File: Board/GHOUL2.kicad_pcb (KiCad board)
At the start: 2 copper layers, 105.1 x 68.6 mm, 16 parts, among them J1 Conn_01x02, Q1 IRF540N, Q2 IRF540N, U1 Teensy3.5_All_Pins, U10 GHOULIMU, U2 LM7805_TO220, U3 BMP280, U4 Feedback_Serv, U5 LM1084-ADJ, U6 NichromeConnector, U7 Ultimate_GPS_Breakout_v3, U8 Xbee, U9 NichromeConnector

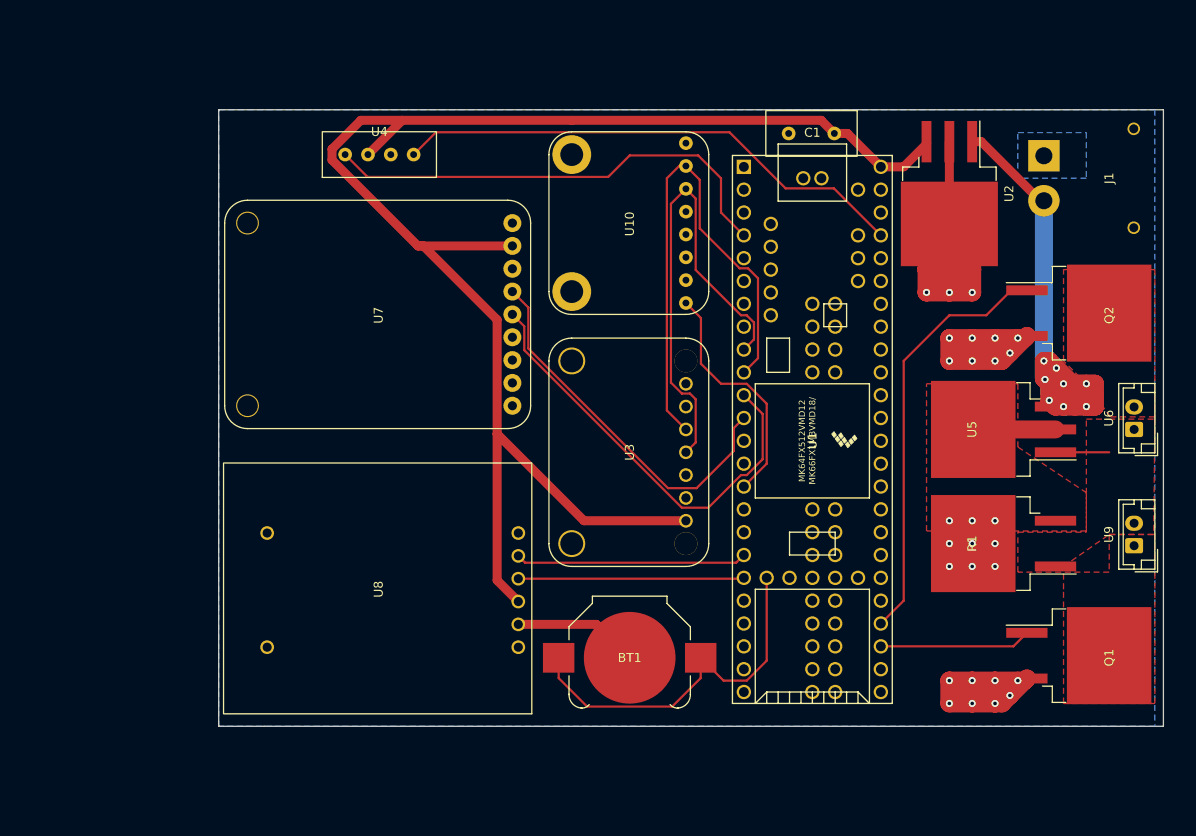
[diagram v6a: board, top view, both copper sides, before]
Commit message: Rounded Corners but not mounting holes
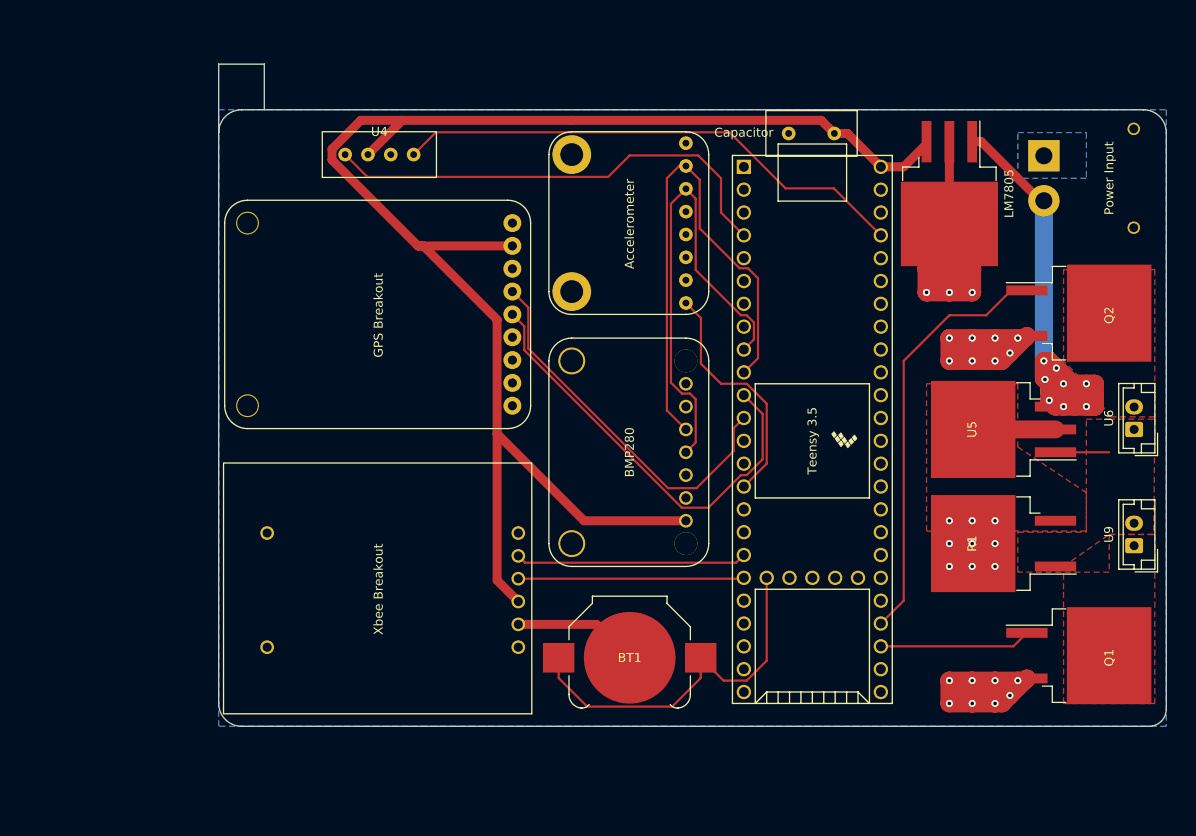
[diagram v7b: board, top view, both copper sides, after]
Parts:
- GPS Breakout: renamed from U7
- Power Input: renamed from J1
- Teensy 3.5: renamed from U1
- Xbee Breakout: renamed from U8
- renumbered U10 to Accelerometer, U3 to BMP280, C1 to Capacitor, U2 to LM7805
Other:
- board size 105.1 x 68.6 mm -> 105.4 x 73.7 mm

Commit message: Added mounting, labels, rounded corners
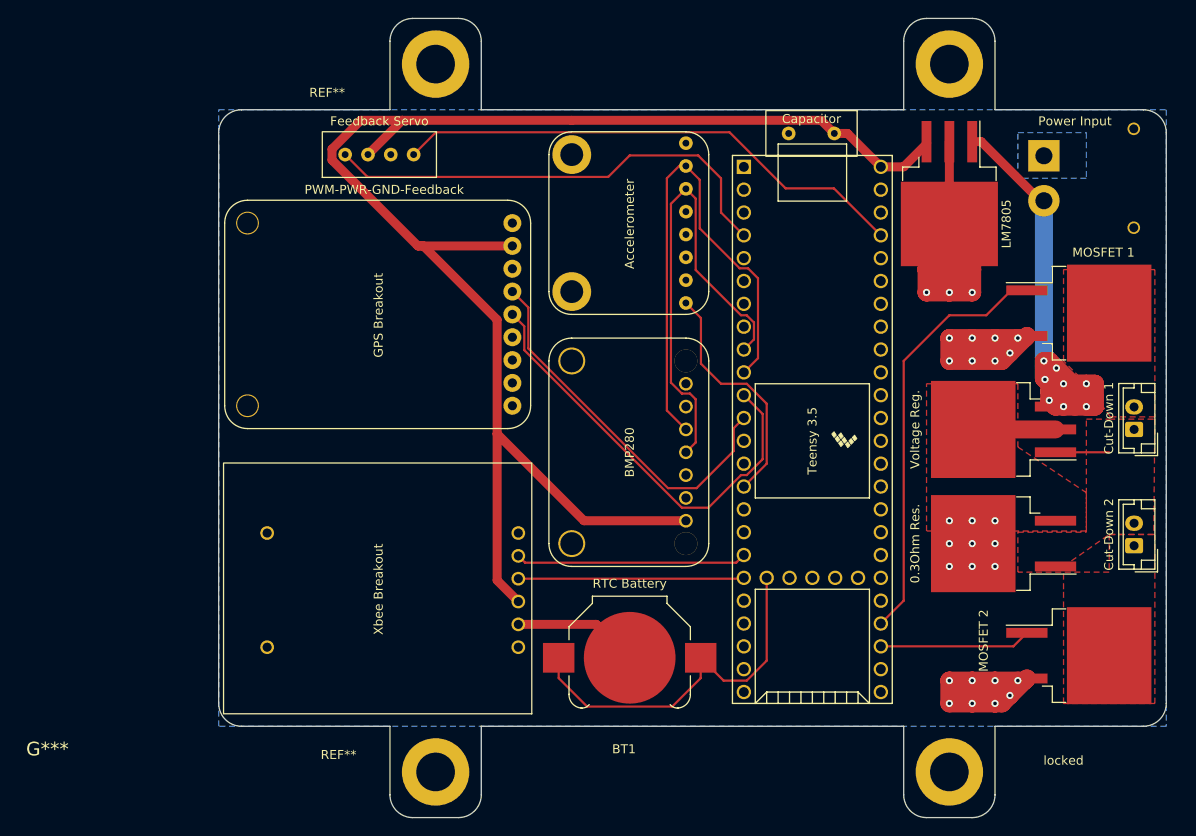
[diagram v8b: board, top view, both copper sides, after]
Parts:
- added ?: , , F.Cu at (175.3, 63.5)
- added G***: LOGO, GHOULFootPrints:GHOULFootprint, F.Cu at (123.2, 109.2)
- added REF**: MountingHole_4.3mm_M4_DIN965_Pad, mechanical:MountingHole_4.3mm_M4_DIN965_Pad, F.Cu at (118.1, 63.5)
- added REF**: MountingHole_4.3mm_M4_DIN965_Pad, mechanical:MountingHole_4.3mm_M4_DIN965_Pad, F.Cu at (118.1, 142.2)
- added locked: MountingHole_4.3mm_M4_DIN965_Pad, mechanical:MountingHole_4.3mm_M4_DIN965_Pad, F.Cu at (175.3, 142.2)
- 0.3Ohm Res.: renamed from R1
- Cut-Down 1: renamed from U6
- Cut-Down 2: renamed from U9
- Feedback Servo: renamed from U4
- MOSFET 1: renamed from Q2
- MOSFET 2: renamed from Q1
- Voltage Reg.: renamed from U5
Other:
- board size 105.4 x 73.7 mm -> 105.4 x 88.9 mm
- board text added: "PWM-PWR-GND-Feedback"
- board text added: "RTC Battery"
- board text added: "Resources Available Online: bpp.umd.edu https://github.com/UMDBPP/GHOUL"
- board text added: "Venting makes me feel good"
- board text added: "Version 2.0 HAB Helium Venting Board Produced by: Michael Kalin, Kruti Bhingradiya, Jeremy Kuznetsov, Daniel Grammer, and Akemi Takeuchi Univ. of Maryland, College Park (2023)"
